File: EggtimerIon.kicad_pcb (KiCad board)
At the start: 4 copper layers, 45 x 30 mm, 46 parts, among them J1 Conn_01x02, J2 Conn_01x03, J3 B2B-PH-K-S, J4 USB_C_Receptacle_USB2.0, Q1 IRLML6244, Q2 2N7002, Q3 2N7002, U1 ESP32-WROOM-32-N4, U2 MPU-6050, U3 MS5611-01BA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

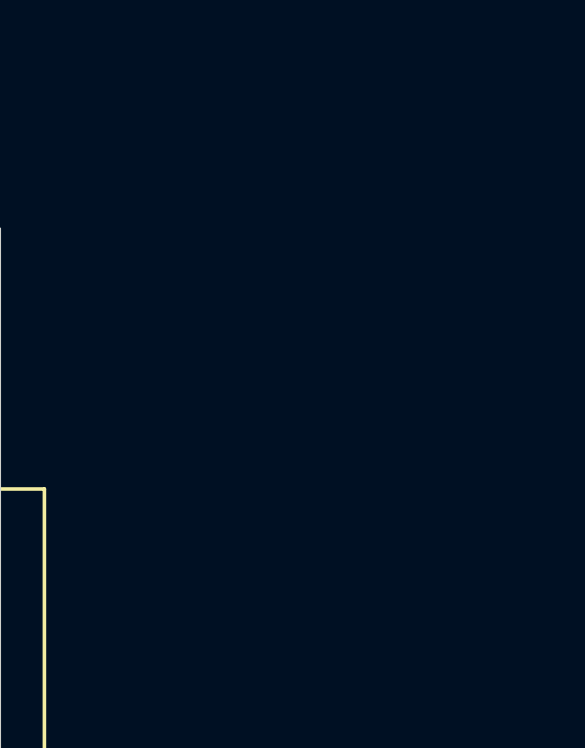
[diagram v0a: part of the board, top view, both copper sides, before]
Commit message: Removed Bridge and Flash
Deleted USB C Connector
Deleted EEPROM
Deleted USB to UART Bridge and external circuitry
Added mounting holes
Added changes to layout
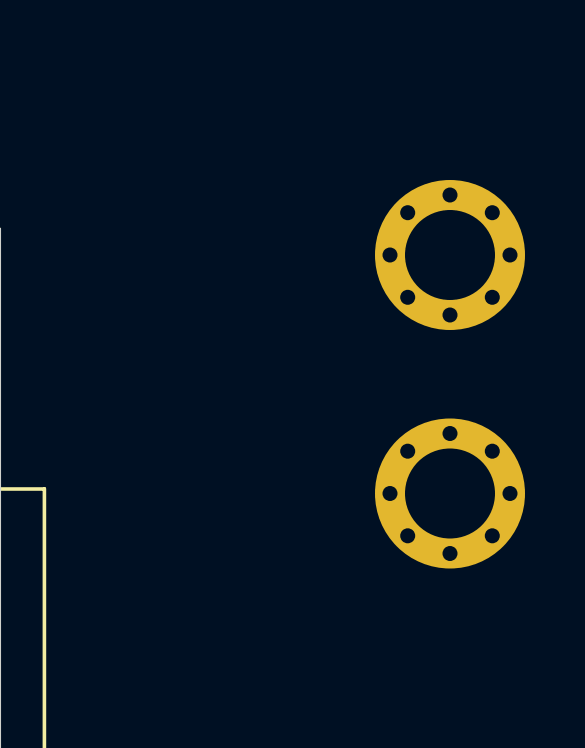
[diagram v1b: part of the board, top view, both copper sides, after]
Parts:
- added H1: MountingHole, PCM_JLCPCB:Hole, 3mm, F.Cu at (195.7, 86.2)
- added H2: MountingHole, PCM_JLCPCB:Hole, 3mm, F.Cu at (195.7, 94.2)

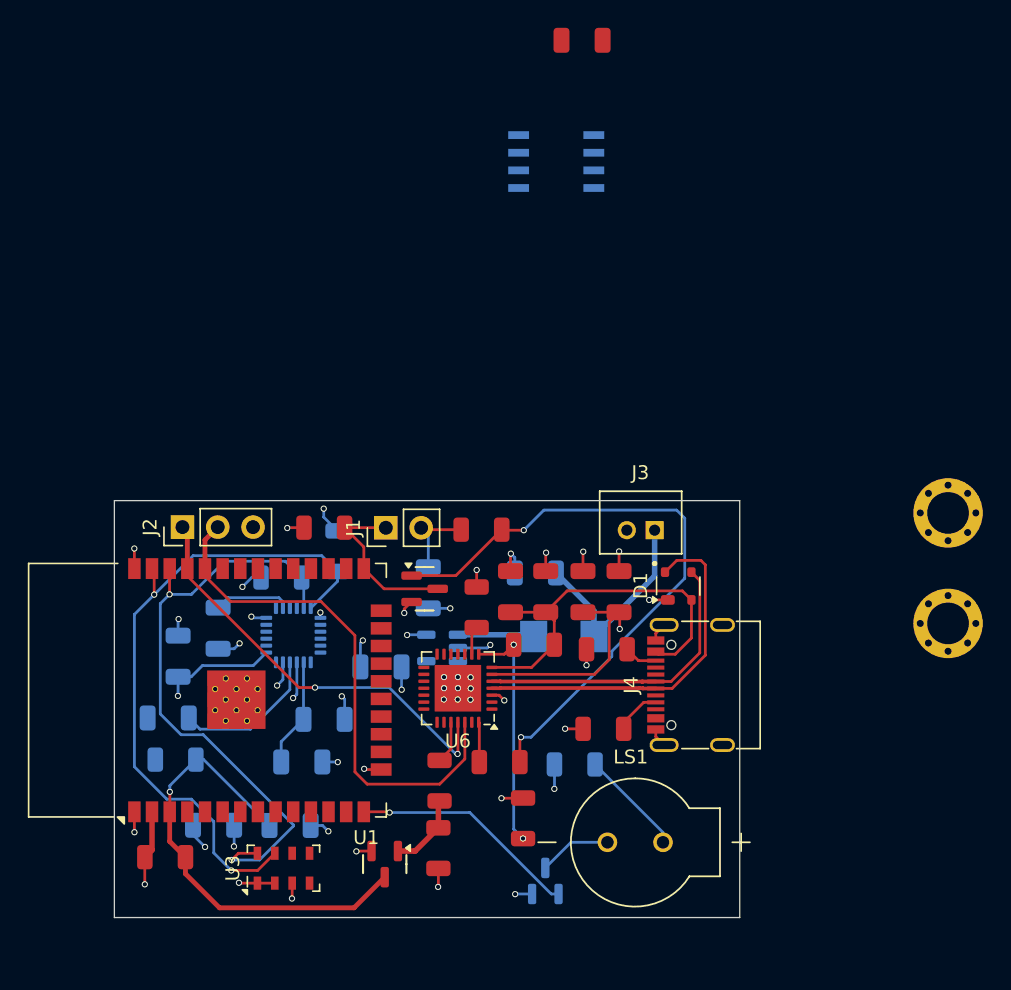
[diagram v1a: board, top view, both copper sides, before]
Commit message: Refined Layout
Removed addditional parts
Shifted MPU6050 to front
Shifted Transistor and LDO to front
Added 3D models for MPU6050 and MBRS diode
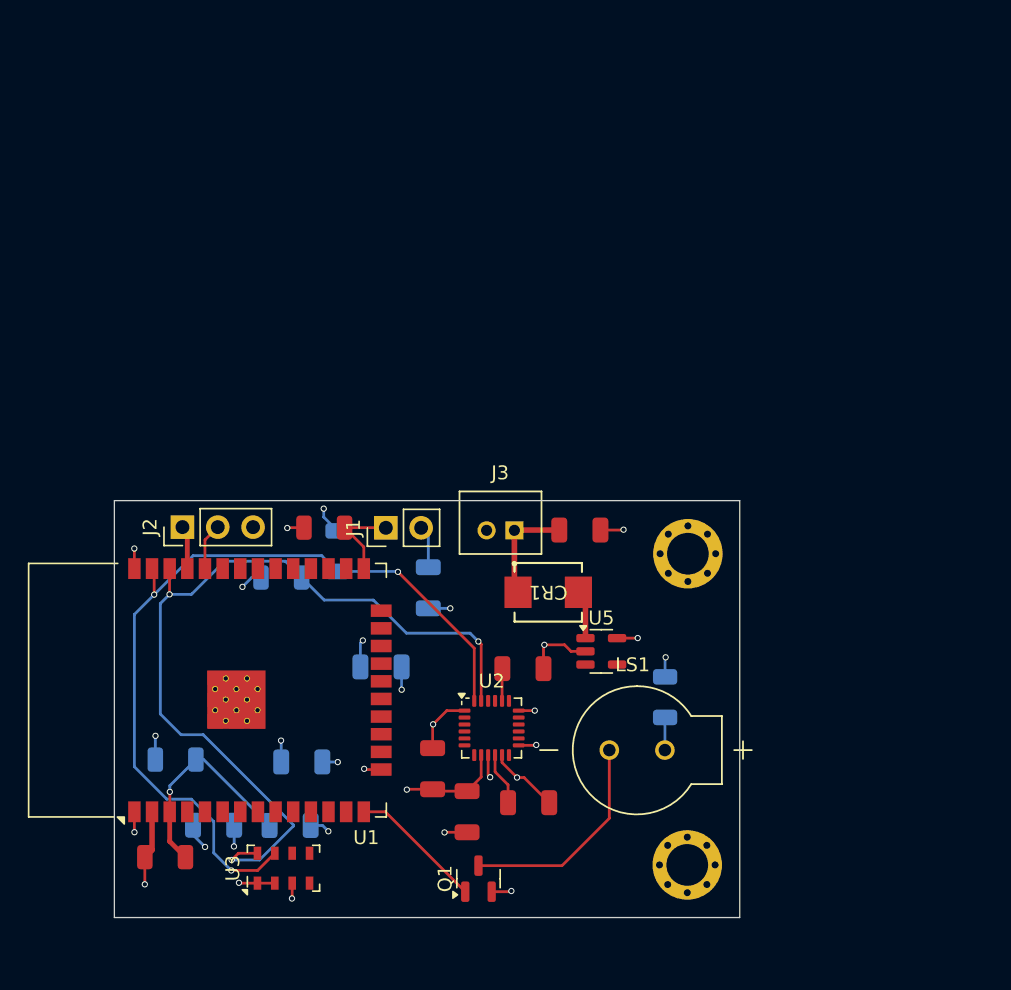
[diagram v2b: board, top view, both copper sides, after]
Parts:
- removed C12, C14: 4.7uF, PCM_JLCPCB:C_1206
- removed C13, C15, C9: 0.1uF, PCM_JLCPCB:C_1206
- removed D1: SP0503BAHT, Package_TO_SOT_SMD:SOT-143
- removed J4: USB_C_Receptacle_USB2.0, Connector_USB:USB_C_Receptacle_G-Switch_GT-USB-7010ASV
- removed Q2, Q3: 2N7002, PCM_JLCPCB:Q_SOT-23
- removed R12, R15: 100, PCM_JLCPCB:R_1206
- removed R13, R14: 100k, PCM_JLCPCB:R_1206
- removed R5: 1k, PCM_JLCPCB:R_1206
- removed R6: 22k1, PCM_JLCPCB:R_1206
- removed R7: 47k5, PCM_JLCPCB:R_1206
- removed R8, R9: 5k1, PCM_JLCPCB:R_1206
- removed U4: CAT24C512XI-T2, CAT24C512:SOIC8_ONS
- removed U6: CP2102N-Axx-xQFN28, Package_DFN_QFN:QFN-28-1EP_5x5mm_P0.5mm_EP3.35x3.35mm
- C10, C4, C5, C6, C7, CR1, Q1, U2, U5: moved to F.Cu
- moved C7 26.6 mm to (165.5, 107.1), turned to 0 degrees
- moved H2 25.6 mm to (176.9, 111.5)
- moved C5 23.6 mm to (161.1, 107.7), turned to 90 degrees
- moved C6 22.1 mm to (165.1, 97.4), turned to 0 degrees
- moved H1 18.9 mm to (177.0, 89.1)
- moved U2 15.7 mm to (162.8, 101.7), turned to 0 degrees
- moved U5 11.5 mm to (170.7, 96.2), turned to 0 degrees
- moved J3 10.1 mm to (163.5, 86.9)
- moved C4 8.58 mm to (158.6, 104.6), turned to -90 degrees
- moved R4 8.11 mm to (175.3, 99.5), turned to -90 degrees
- moved LS1 6.64 mm to (173.3, 103.3)
- moved Q1 4.81 mm to (161.9, 112.5)
- moved C10 4.45 mm to (169.2, 87.4), turned to 0 degrees
- moved CR1 3.38 mm to (166.9, 91.9), turned to 180 degrees
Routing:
- net Net-(Q2-G): track 44.8 -> 0.00 mm, vias 2 -> 0
- net /RXD0: track 37.9 -> 3.37 mm
- net /TXD0: track 30.7 -> 3.13 mm, vias 2 -> 0
- net VBUS: track 27.5 -> 0.00 mm
- net /USB_D+: track 26.3 -> 0.00 mm
- net +3V3: track 54.7 -> 32.5 mm, vias 13 -> 14
- net /USB_D-: track 21.9 -> 0.00 mm
- net /EN: track 33.0 -> 15.5 mm
- net Net-(U6-VBUS): track 17.0 -> 0.00 mm, vias 2 -> 0
- net /SCL: track 44.5 -> 61.2 mm, vias 2 -> 3
- net GND: track 51.6 -> 36.8 mm, vias 38 -> 16
- net /SDA: track 48.2 -> 60.7 mm, vias 2 -> 3
- net Net-(Q1-D): track 5.23 -> 15.7 mm
- net BAT+: track 15.2 -> 7.81 mm
- net Net-(U2-REGOUT): track 10.8 -> 3.81 mm
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
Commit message: Major Updates
- Moved all components to front side
- Added third mounting hole
- Added most JLC #'s to components
- Replaced buzzer with one in stock
- Changed passive components from 1206 to 0402 for assembly
- Replaced components based on schematic
- Added zones for power and ground pours
- Routed tracks and vias
- Removed designator silk and added labels to jumper pins
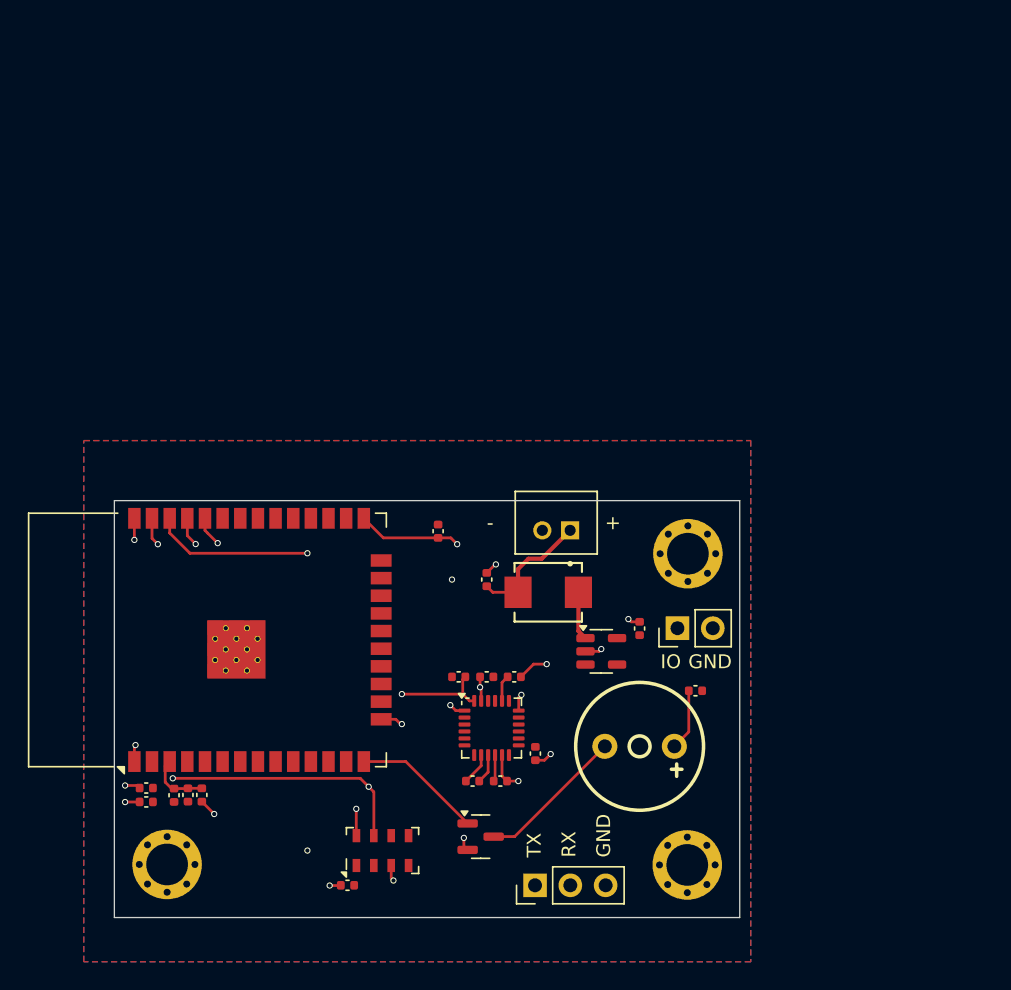
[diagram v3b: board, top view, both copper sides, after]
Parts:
- added H3: MountingHole, PCM_JLCPCB:Hole, 3mm, F.Cu at (139.5, 111.5)
- C1, C11, C2, C3, C8: footprint PCM_JLCPCB:C_1206 -> Capacitor_SMD:C_0402_1005Metric; moved to F.Cu
- C10, C4, C5, C6, C7: footprint PCM_JLCPCB:C_1206 -> Capacitor_SMD:C_0402_1005Metric
- LS1: value AT-1127-ST-2-R -> HNB09A03; footprint AT-1127-ST-2-R:XDCR_AT-1127-ST-2-R -> HNB09A03:HNB09A03
- R1, R2, R3, R4: footprint PCM_JLCPCB:R_1206 -> Capacitor_SMD:C_0402_1005Metric; moved to F.Cu
- R10, R11: footprint PCM_JLCPCB:R_1206 -> Capacitor_SMD:C_0402_1005Metric
- moved J2 36.2 mm to (166.0, 113.0)
- moved J1 22.2 mm to (176.2, 94.5)
- moved R3 16.4 mm to (162.5, 98.0), turned to 180 degrees
- moved C8 15.9 mm to (152.5, 113.0)
- moved C11 15.5 mm to (173.5, 94.5)
- moved R2 12.6 mm to (160.5, 98.0), turned to 0 degrees
- moved C1 11.3 mm to (138.0, 106.0), turned to 0 degrees
- moved R10 8.19 mm to (159.0, 87.5), turned to -90 degrees
- moved C10 7.59 mm to (162.5, 91.0), turned to 90 degrees
- moved U3 7.24 mm to (155.0, 110.5)
- moved C3 6.72 mm to (142.0, 106.5), turned to 90 degrees
- moved C5 6.46 mm to (166.0, 103.5)
- moved C2 5.13 mm to (138.0, 107.0)
- moved R11 4.50 mm to (140.0, 106.5), turned to 90 degrees
- moved J3 4.01 mm to (167.5, 86.9)
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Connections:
- R4 pad 2: Net-(LS1-PadP) -> Net-(LS1-Pad1)
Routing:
- net /RXD0: track 3.37 -> 46.9 mm, vias 0 -> 2
- net /TXD0: track 3.13 -> 46.1 mm, vias 0 -> 2
- net +3V3: track 32.5 -> 2.33 mm, vias 14 -> 0
- net /IO0: track 6.49 -> 25.8 mm, vias 0 -> 1
- net /SCL: track 61.2 -> 48.7 mm
- net /EN: track 15.5 -> 4.45 mm, vias 1 -> 0
- net /SDA: track 60.7 -> 51.7 mm, vias 3 -> 4
- net GND: track 36.8 -> 30.4 mm, vias 16 -> 17
- net Net-(Q1-D): track 15.7 -> 10.3 mm
- net Net-(LS1-Pad1): track 0.00 -> 4.81 mm
- net Net-(LS1-PadP): track 2.36 -> 0.00 mm
- net Net-(U2-REGOUT): track 3.81 -> 1.91 mm
- net BAT+: track 7.81 -> 9.00 mm
- added copper zone on F.Cu, net +3V3
- added copper zone on B.Cu, net GND
- added copper zone on In2.Cu, net GND
- removed copper zone on In2.Cu, net +3V3
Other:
- board text added: "+"
- board text added: "-"
- board text added: "GND"
- board text added: "IO"
- board text added: "RX"
- board text added: "TX"
